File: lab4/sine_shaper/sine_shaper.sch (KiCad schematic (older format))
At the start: 30 parts, among them J1 Conn_01x02_Male, J2 Screw_Terminal_01x03, J3 Conn_01x02_Male, Q1 MMBT3904, Q2 MMBT3904, Q3 MMBT3904, U1 LM358

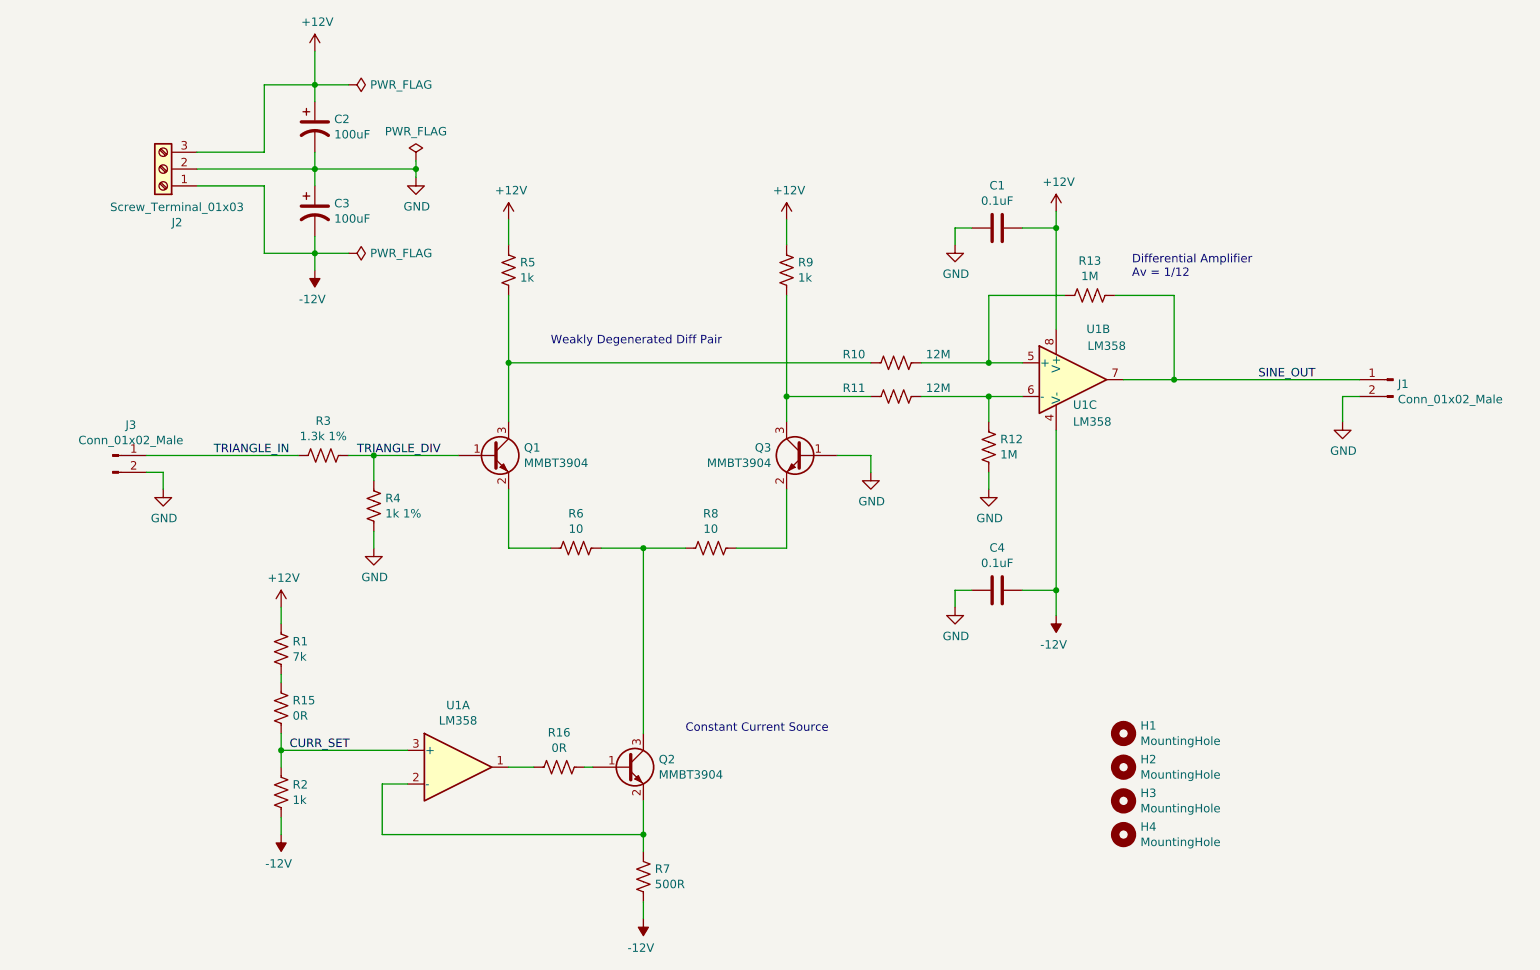
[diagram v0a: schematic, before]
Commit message: Finish function generator
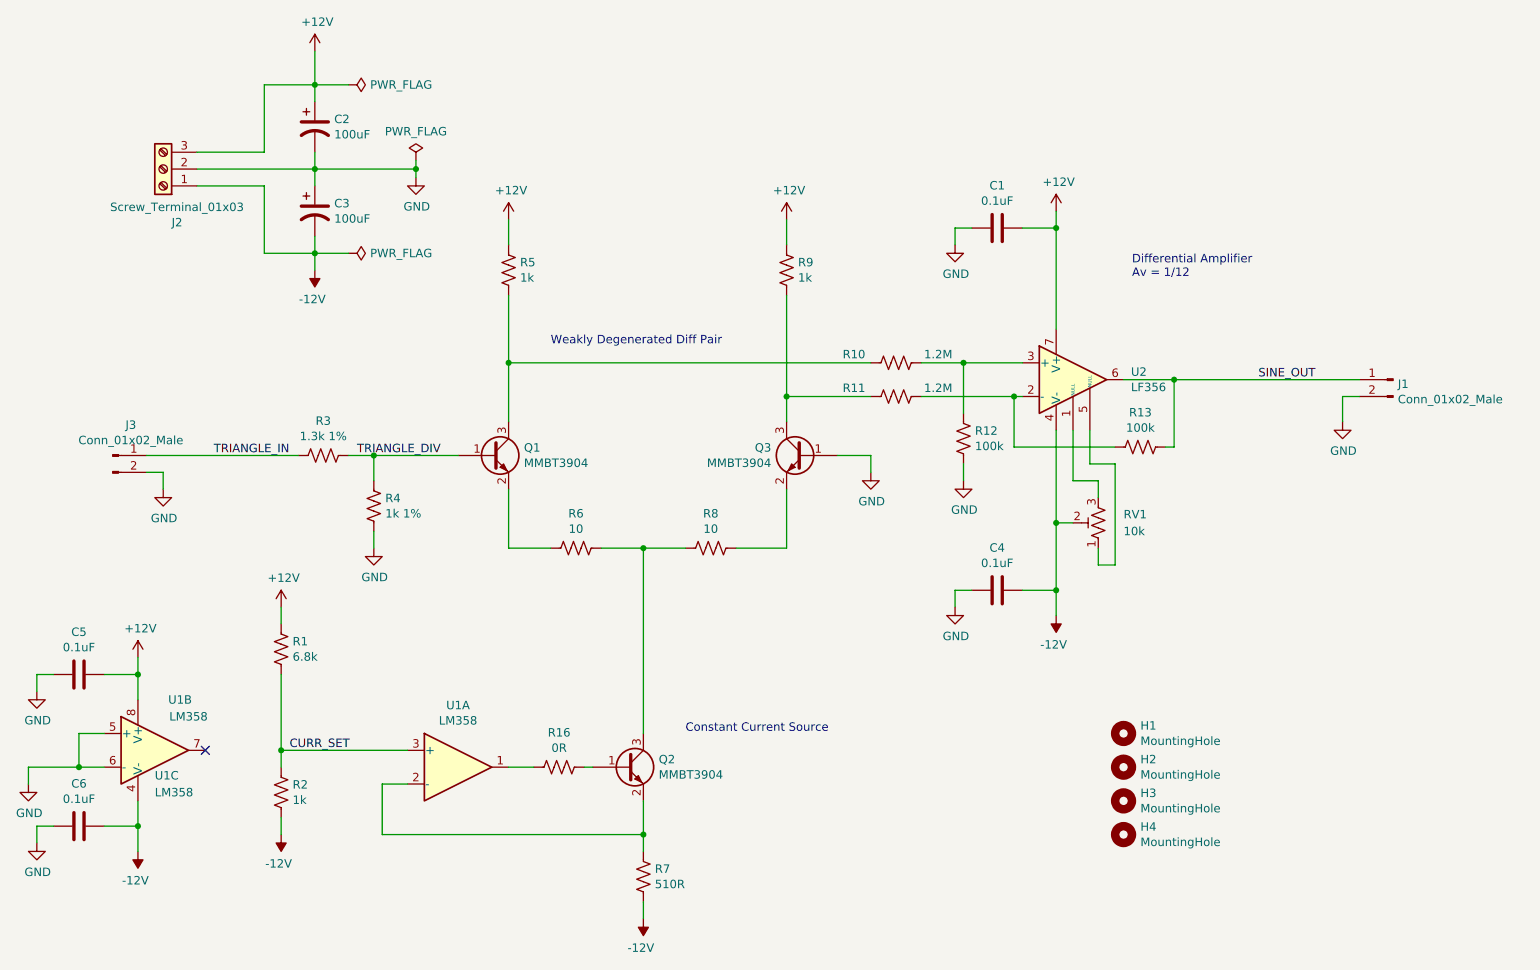
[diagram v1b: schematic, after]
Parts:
- removed R15: 0R, Resistor_SMD:R_0805_2012Metric, symbol Device:R_US
- added C5, C6: 0.1uF, Capacitor_SMD:C_0805_2012Metric, symbol Device:C
- added RV1: 10k, Potentiometer_THT:Potentiometer_Bourns_3296W_Vertical, symbol Device:R_POT_TRIM_US
- added U2: LF356, Package_DIP:DIP-8_W7.62mm, symbol Amplifier_Operational:LF356
- R1: value 7k -> 6.8k
- R10, R11: value 12M -> 1.2M
- R12, R13: value 1M -> 100k
- R7: value 500R -> 510R
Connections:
- net +12V: now also C5.1, U2.7 (V+)
- net -12V: now also C6.1, RV1.2, U2.4 (V-)
- net CURR_SET: now also R1.2
- net GND: now also U1.5 (+), U1.6 (-), C5.2, C6.2
- net SINE_OUT: now also U2.6; no longer U1.7
- new net: R10.1, R12.2, U2.3 (+)
- new net: R11.1, R13.1, U2.2 (-)
- new net: RV1.3, U2.1 (NULL)
- new net: RV1.1, U2.5 (NULL)
- no-connect marks 0 -> 1
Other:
- moved on the sheet: R12, R13, U1B, U1C
